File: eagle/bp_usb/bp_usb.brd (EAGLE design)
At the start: 77.6 x 26.6 mm, 13 parts, among them J1 111-0703-001, J2 111-0702-001, J3 111-0703-001, J4 111-0702-001, J5 TSM-105-01-S-SV

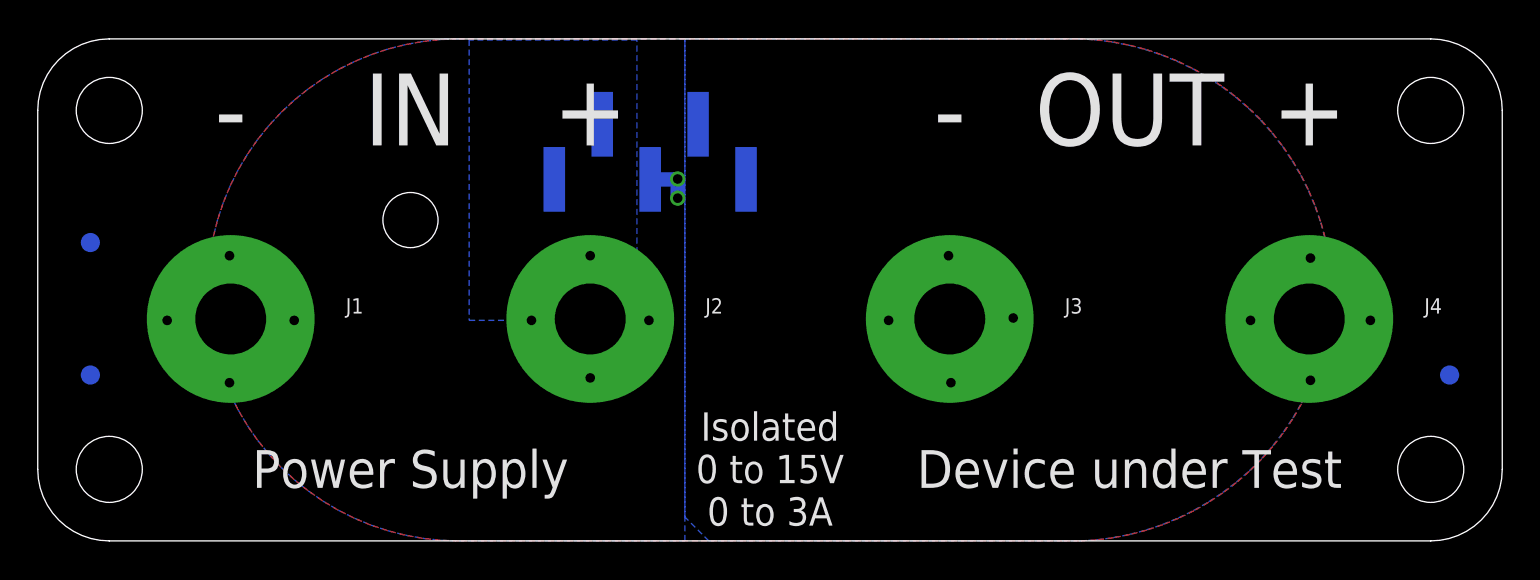
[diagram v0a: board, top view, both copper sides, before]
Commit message: Pre-production update.
* Increased clearances from chassis/enclosure ground.
* Improved text.
* Added gerbers.
* Added USB back panel.
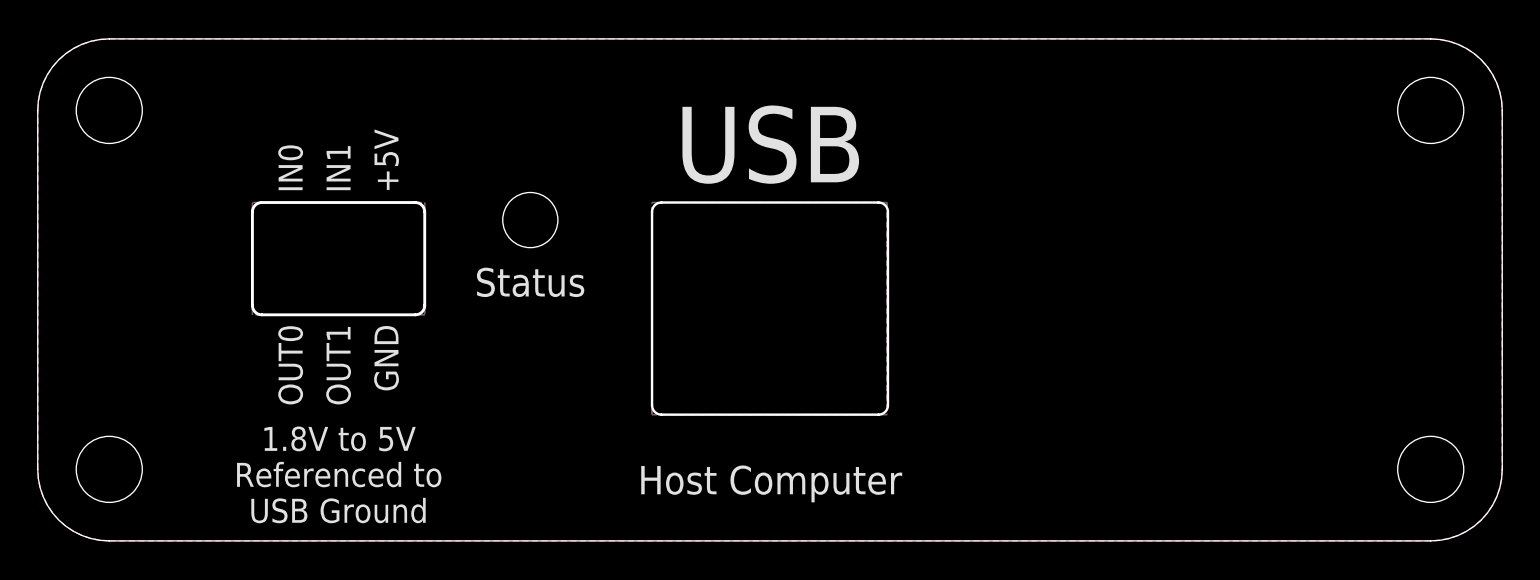
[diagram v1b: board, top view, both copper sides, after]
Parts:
- removed FUD1, FUD2, FUD3: FIDUCIAL_1MM, jetperch:FIDUCIAL_1MM_2MM
- removed H3, H4, H5: HOLE_#6, jetperch:HOLE_3.5MM
- removed J1, J3: 111-0703-001, jetperch:BINDING_POST_6
- removed J2, J4: 111-0702-001, jetperch:BINDING_POST_6
- removed J5: TSM-105-01-S-SV, jetperch:CONN_0.1_5X1_MS
- H2: value HOLE_#6 -> ZUSANSR-F-2; device jetperch:HOLE_3.5MM -> jetperch:FOAM_0.5_0.25
- moved H2 51.7 mm to (54.0, 16.0), flipped to the bottom
- moved H1 6.35 mm to (26.1, 17.0)
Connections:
- removed net EXT_IN: J2.1, J5.1, J5.2
- removed net EXT_NEG: J1.1, J3.1, J5.3
- removed net EXT_OUT: J4.1, J5.4, J5.5
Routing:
- net EXT_NEG: track 29.4 -> 0.00 mm, vias 10 -> 0
- net EXT_OUT: track 12.9 -> 0.00 mm, vias 4 -> 0
- net EXT_IN: track 12.8 -> 0.00 mm, vias 4 -> 0
- removed copper zone on layer 16, net EXT_IN
- removed copper zone on layer 16, net EXT_OUT
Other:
- outline, holes or cut-outs redrawn
- board text added: "1.8V to 5V Referenced to USB Ground"
- board text added: "Host Computer"
- board text added: "IN0 IN1 +5V"
- board text added: "Joulescope Back Panel: rev G 2019 Jetperch LLC"
- board text added: "OUT0 OUT1 GND"
- board text added: "Status"
- board text added: "USB"
- board text removed: "+"
- board text removed: "-"
- board text removed: "All dimensions in millimeters"
- board text removed: "Device under Test"
- board text removed: "IN"
- board text removed: "Isolated 0 to 15V 0 to 3A"
- board text removed: "Joulescope Front Panel: Binding Posts rev B 2019 Jetperch LLC"
- board text removed: "OUT"
- board text removed: "Power Supply"

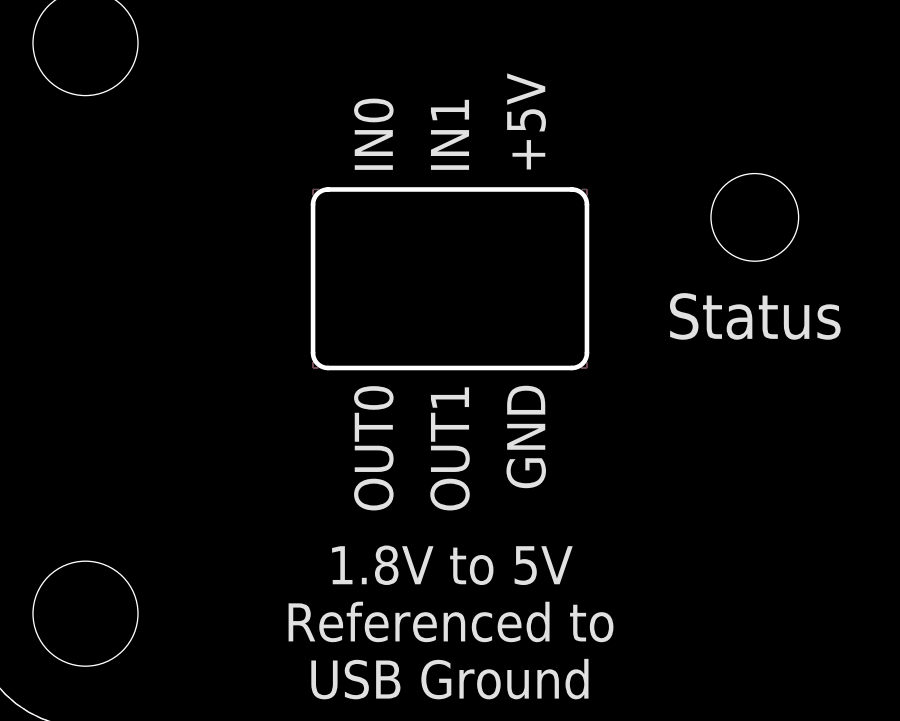
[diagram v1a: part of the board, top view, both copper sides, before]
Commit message: Modified USB back panel to move GPI/O cutout and fixed schematic file name.
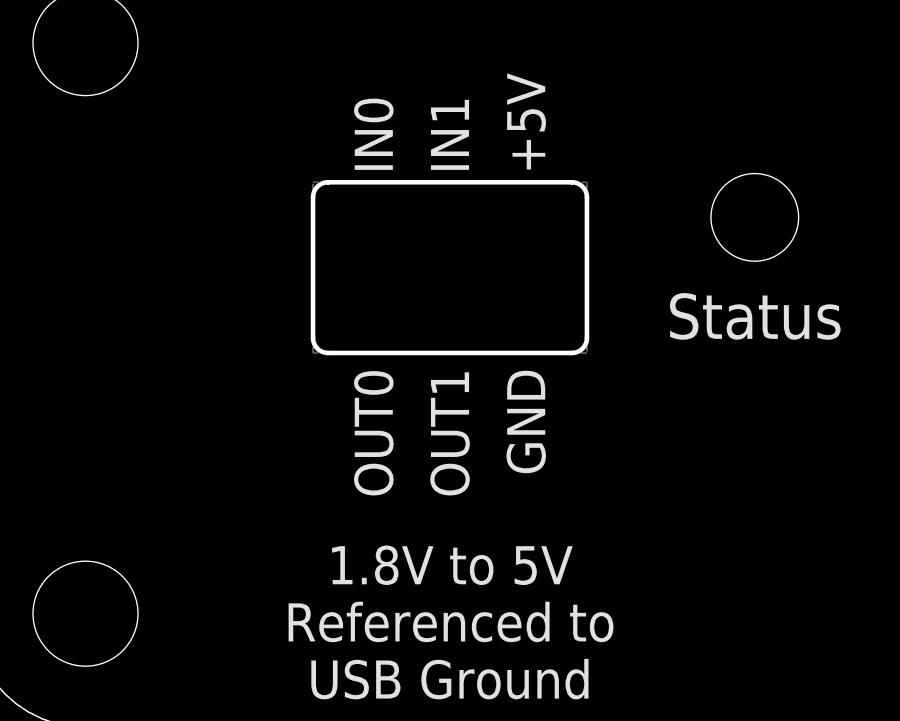
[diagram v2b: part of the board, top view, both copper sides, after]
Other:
- outline, holes or cut-outs redrawn
- board text added: "Joulescope Back Panel: rev H 2019 Jetperch LLC"
- board text removed: "Joulescope Back Panel: rev G 2019 Jetperch LLC"
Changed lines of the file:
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@@
 <?xml version="1.0" encoding="utf-8"?>
 <!DOCTYPE eagle SYSTEM "eagle.dtd">
-<eagle version="9.3.2">
+<eagle version="9.4.0">
 <drawing>
 <settings>
@@
 <grid distance="1" unitdist="mm" unit="mm" style="lines" multiple="1" display="no" altdistance="0.1" altunitdist="mm" altunit="mm"/>
 <layers>
-<layer number="1" name="Top" color="4" fill="1" visible="yes" active="yes"/>
+<layer number="1" name="Top" color="4" fill="1" visible="no" active="yes"/>
 <layer number="2" name="Route2" color="1" fill="3" visible="no" active="no"/>
 <layer number="15" name="Route15" color="4" fill="6" visible="no" active="no"/>
-<layer number="16" name="Bottom" color="1" fill="1" visible="yes" active="yes"/>
+<layer number="16" name="Bottom" color="1" fill="1" visible="no" active="yes"/>
 <layer number="17" name="Pads" color="2" fill="1" visible="yes" active="yes"/>
 <layer number="18" name="Vias" color="2" fill="1" visible="yes" active="yes"/>
@@
 <hole x="73.81" y="22.81" drill="3.5"/>
 <text x="38.8" y="21" size="4" layer="121" font="vector" ratio="20" align="center">USB</text>
-<text x="38.8" y="3.01" size="1.27" layer="122" font="vector" ratio="20" rot="MR0" align="center">Joulescope Back Panel: rev G
+<text x="38.8" y="3.01" size="1.27" layer="122" font="vector" ratio="20" rot="MR0" align="center">Joulescope Back Panel: rev H
 2019 Jetperch LLC</text>
 <dimension x1="0" y1="22.81" x2="77.6" y2="19.05" x3="38.8" y3="37.75" textsize="1.778" layer="47" dtype="horizontal"/>
@@
 <wire x1="0" y1="18.3" x2="23.6" y2="18.3" width="0.127" layer="22" style="shortdash"/>
 <wire x1="58" y1="19.3" x2="77.6" y2="19.3" width="0.254" layer="22"/>
-<wire x1="20.005" y1="11.98" x2="11.875" y2="11.98" width="0.1524" layer="20"/>
-<wire x1="11.875" y1="11.98" x2="11.375" y2="12.48" width="0.1524" layer="20" curve="-90"/>
-<wire x1="11.375" y1="12.48" x2="11.375" y2="17.43" width="0.1524" layer="20"/>
-<wire x1="11.375" y1="17.43" x2="11.875" y2="17.93" width="0.1524" layer="20" curve="-90"/>
-<wire x1="11.875" y1="17.93" x2="20.005" y2="17.93" width="0.1524" layer="20"/>
-<wire x1="20.005" y1="17.93" x2="20.505" y2="17.43" width="0.1524" layer="20" curve="-90"/>
-<wire x1="20.505" y1="17.43" x2="20.505" y2="12.48" width="0.1524" layer="20"/>
-<wire x1="20.505" y1="12.48" x2="20.005" y2="11.98" width="0.1524" layer="20" curve="-90"/>
+<wire x1="11.375" y1="12.98" x2="11.375" y2="17.67" width="0.1524" layer="20"/>
+<wire x1="11.375" y1="17.67" x2="11.875" y2="18.17" width="0.1524" layer="20" curve="-90"/>
+<wire x1="11.875" y1="18.17" x2="20.005" y2="18.17" width="0.1524" layer="20"/>
+<wire x1="20.005" y1="18.17" x2="20.505" y2="17.67" width="0.1524" layer="20" curve="-90"/>
+<wire x1="20.505" y1="17.67" x2="20.505" y2="12.98" width="0.1524" layer="20"/>
+<wire x1="20.505" y1="12.98" x2="20.005" y2="12.48" width="0.1524" layer="20" curve="-90"/>
+<wire x1="20.005" y1="12.48" x2="11.875" y2="12.48" width="0.1524" layer="20"/>
+<wire x1="11.875" y1="12.48" x2="11.375" y2="12.98" width="0.1524" layer="20" curve="-90"/>
 <text x="15.94" y="18.43" size="1.27" layer="121" font="vector" ratio="20" distance="100" rot="SR90" align="center-left">IN0
 IN1
 +5V</text>
-<text x="15.94" y="11.48" size="1.27" layer="121" font="vector" ratio="20" distance="100" rot="SR90" align="center-right">OUT0
+<text x="15.94" y="11.98" size="1.27" layer="121" font="vector" ratio="20" distance="100" rot="SR90" align="center-right">OUT0
 OUT1
 GND</text>
 <dimension x1="0" y1="22.81" x2="38.8" y2="19.05" x3="19.4" y3="32.75" textsize="1.778" layer="47" dtype="horizontal"/>
-<dimension x1="15.94" y1="11.48" x2="38.8" y2="6.19" x3="27.37" y3="-4.37" textsize="1.778" layer="47" dtype="horizontal"/>
+<dimension x1="15.94" y1="11.98" x2="38.8" y2="6.19" x3="27.37" y3="-4.37" textsize="1.778" layer="47" dtype="horizontal"/>
 <text x="15.94" y="3.5" size="1.27" layer="121" font="vector" ratio="20" align="center">1.8V to 5V
 Referenced to
@@
 <vertex x="0" y="22.81" curve="-90"/>
 </polygon>
-<polygon width="0.1524" layer="1" pour="cutout">
-<vertex x="11.375" y="17.93"/>
-<vertex x="20.505" y="17.93"/>
-<vertex x="20.505" y="11.98"/>
-<vertex x="11.375" y="11.98"/>
+<polygon width="0.1524" layer="1" spacing="0" pour="cutout">
+<vertex x="11.375" y="18.17"/>
+<vertex x="20.505" y="18.17"/>
+<vertex x="20.505" y="12.48"/>
+<vertex x="11.375" y="12.48"/>
 </polygon>
-<polygon width="0.1524" layer="16" pour="cutout">
-<vertex x="11.375" y="17.93"/>
-<vertex x="20.505" y="17.93"/>
-<vertex x="20.505" y="11.98"/>
-<vertex x="11.375" y="11.98"/>
+<polygon width="0.1524" layer="16" spacing="0" pour="cutout">
+<vertex x="11.375" y="18.17"/>
+<vertex x="20.505" y="18.17"/>
+<vertex x="20.505" y="12.48"/>
+<vertex x="11.375" y="12.48"/>
 </polygon>
 <polygon width="0.1524" layer="1" pour="cutout">

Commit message: Added brief fab notes to back panel PCB design.
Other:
- board text added: "All dimensions in millimeters Place all markings on back (including pcb order number). Add flammability rating marking on back, such as 94V-0. The front-side surface is cosmetic - reject units with scratches and blemishes."
- board text added: "Joulescope Back Panel: rev J 2019 Jetperch LLC"
- board text removed: "Joulescope Back Panel: rev H 2019 Jetperch LLC"
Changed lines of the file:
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@@
 <?xml version="1.0" encoding="utf-8"?>
 <!DOCTYPE eagle SYSTEM "eagle.dtd">
-<eagle version="9.4.0">
+<eagle version="9.5.0">
 <drawing>
 <settings>
@@
 <grid distance="1" unitdist="mm" unit="mm" style="lines" multiple="1" display="no" altdistance="0.1" altunitdist="mm" altunit="mm"/>
 <layers>
-<layer number="1" name="Top" color="4" fill="1" visible="no" active="yes"/>
+<layer number="1" name="Top" color="4" fill="1" visible="yes" active="yes"/>
 <layer number="2" name="Route2" color="1" fill="3" visible="no" active="no"/>
 <layer number="15" name="Route15" color="4" fill="6" visible="no" active="no"/>
@@
 <hole x="73.81" y="22.81" drill="3.5"/>
 <text x="38.8" y="21" size="4" layer="121" font="vector" ratio="20" align="center">USB</text>
-<text x="38.8" y="3.01" size="1.27" layer="122" font="vector" ratio="20" rot="MR0" align="center">Joulescope Back Panel: rev H
+<text x="38.8" y="3.01" size="1.27" layer="122" font="vector" ratio="20" rot="MR0" align="center">Joulescope Back Panel: rev J
 2019 Jetperch LLC</text>
 <dimension x1="0" y1="22.81" x2="77.6" y2="19.05" x3="38.8" y3="37.75" textsize="1.778" layer="47" dtype="horizontal"/>
@@
 <vertex x="56" y="20.3"/>
 </polygon>
+<text x="14" y="-19" size="1.778" layer="153">All dimensions in millimeters
+Place all markings on back (including pcb order number).
+Add flammability rating marking on back, such as 94V-0.
+The front-side surface is cosmetic - reject units with scratches and blemishes.</text>
 </plain>
 <attributes>
